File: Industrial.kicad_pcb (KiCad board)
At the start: 2 copper layers, 101.6 x 39.4 mm, 17 parts, among them J1 ASC712, J2 INA219, J3 Corriente, Q1 TIC106, U1 H11AA1, U2 MOC3052M, U3 Esp32

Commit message: fix pcb
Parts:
- moved Q1 56.9 mm to (194.6, 111.8), turned to 90 degrees
- moved J3 37.3 mm to (175.5, 82.3), turned to 90 degrees
- moved R6 28.1 mm to (181.4, 101.1)
- moved R2 27.5 mm to (153.7, 129.0)
- moved R3 26.8 mm to (167.6, 129.0)
- moved U1 21.8 mm to (160.5, 117.1)
- moved R4 21.6 mm to (181.9, 119.4)
- moved D1 18.3 mm to (181.1, 128.0)
- moved R5 17.4 mm to (165.6, 93.0)
- moved U2 16.1 mm to (167.4, 101.6)
- moved J1 16.0 mm to (161.3, 82.3)
- moved L1 15.2 mm to (197.9, 133.3)
- moved R1 14.5 mm to (154.4, 111.0)
- moved S1 13.8 mm to (141.7, 99.8)
- moved J2 13.4 mm to (138.9, 82.0)
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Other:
- board size 101.6 x 39.4 mm -> 100.3 x 61.7 mm

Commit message: finish first version
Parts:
- removed J3: Corriente, Connector_PinHeader_2.54mm:PinHeader_1x02_P2.54mm_Vertical
- added J4: Corriente, Connector_PinHeader_2.54mm:PinHeader_1x02_P2.54mm_Vertical, F.Cu at (197.4, 97.8)
- Q1: footprint Package_TO_SOT_THT:TO-220-3_Vertical -> TerminalBlock:TerminalBlock_bornier-3_P5.08mm
- moved J1 54.6 mm to (142.5, 133.6)
- moved R2 37.8 mm to (184.7, 107.4), turned to 180 degrees
- moved R4 34.4 mm to (149.6, 107.4), turned to 180 degrees
- moved R1 32.2 mm to (185.4, 119.6), turned to 180 degrees
- moved S1 29.1 mm to (170.7, 97.3), turned to 90 degrees
- moved R5 21.0 mm to (145.0, 88.9), turned to 180 degrees
- moved R3 19.1 mm to (150.1, 121.4), turned to 180 degrees
- moved U2 17.0 mm to (152.9, 92.7)
- moved R6 16.8 mm to (165.4, 106.2), turned to 180 degrees
- moved J2 15.5 mm to (154.4, 81.3)
- moved D1 9.41 mm to (171.7, 128.5)
- moved U1 7.68 mm to (166.9, 121.4), turned to 180 degrees
- moved Q1 5.40 mm to (198.1, 115.8)
- moved U3 1.83 mm to (117.9, 103.1)
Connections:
- net /notA renamed Net-(S1-Pad2)
- J2 pad 1: /Vcc -> /5v
- Q1 pad 1: /Battery -> Net-(J4-Pad1)
- S1 pad 1: /Vcc -> Net-(S1-Pad1)
- S1 pad 16: Net-(S1-Pad16) -> /5v
- U3 pad 32: Net-(U3-Pad32) -> GND
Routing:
- net /5v: track 0.00 -> 251.2 mm
- net GND: track 0.00 -> 212.7 mm, vias 0 -> 2
- net /Fase: track 0.00 -> 94.2 mm, vias 0 -> 2
- net /Vcc: track 0.00 -> 87.0 mm
- net /TrueZero: track 0.00 -> 70.1 mm, vias 0 -> 2
- net /Shoot: track 0.00 -> 65.0 mm
- net /ZeroCross: track 0.00 -> 54.7 mm
- net /Neutro: track 0.00 -> 50.8 mm
- net Net-(D1-Pad1): track 0.00 -> 47.9 mm
- net /SDA: track 0.00 -> 41.8 mm, vias 0 -> 2
- net /SCR: track 0.00 -> 35.5 mm
- net /SCL: track 0.00 -> 33.1 mm, vias 0 -> 2
- net Net-(R1-Pad1): track 0.00 -> 32.3 mm
- net /A0: track 0.00 -> 32.3 mm
- net Net-(R2-Pad1): track 0.00 -> 30.1 mm
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- added copper zone on B.Cu, net GND
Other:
- net class Juanda added: clearance 0.3, trace_width 0.9, via_dia 1, via_drill 0.8
- net class power added: clearance 0.4, trace_width 1.27, via_dia 1, via_drill 0.8
- net class señal added: clearance 0.3, trace_width 0.762, via_dia 1, via_drill 0.8
- board text added: "Cargador de baterias"
- board text added: "Ingenieria Electrónica UPB Juan David Barrero Luis David Calderon"

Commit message: finish but it can be better
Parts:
- added C1: 1000uF, Capacitor_THT:CP_Radial_D13.0mm_P5.00mm, F.Cu at (162.6, 142.2)
- added D2: D, Diode_THT:D_A-405_P7.62mm_Horizontal, F.Cu at (178.1, 145.8)
- added D3: LED, LED_THT:LED_D4.0mm, F.Cu at (108.0, 141.8)
- added J3: Conn_01x02, Connector_PinHeader_2.54mm:PinHeader_1x02_P2.54mm_Vertical, F.Cu at (134.4, 140.2)
- added R7: 440, Resistor_THT:R_Axial_DIN0309_L9.0mm_D3.2mm_P5.08mm_Vertical, F.Cu at (120.4, 142.7)
- added U4: LM7805_TO220, Package_TO_SOT_THT:TO-220-3_Vertical, F.Cu at (149.6, 133.3)
- moved J1 12.8 mm to (144.3, 146.3)
- moved L1 12.3 mm to (196.3, 145.5)
- moved Q1 5.86 mm to (196.3, 121.4)
- moved D1 5.73 mm to (177.3, 129.8)
- moved BT1 1.27 mm to (196.3, 87.4)
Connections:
- net Net-(D1-Pad1) renamed /bridge
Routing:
- net /5v: track 251.2 -> 132.9 mm, vias 0 -> 2
- net /Fase: track 94.2 -> 177.5 mm
- net Net-(C1-Pad1): track 0.00 -> 39.8 mm
- net /TrueZero: track 70.1 -> 103.7 mm, vias 2 -> 0
- net Net-(J3-Pad2): track 0.00 -> 33.1 mm
- net GND: track 212.7 -> 242.8 mm, vias 2 -> 4
- net /A0: track 32.3 -> 60.1 mm, vias 0 -> 2
- net /Shoot: track 65.0 -> 41.5 mm, vias 0 -> 2
- net /Vcc: track 87.0 -> 108.7 mm
- net /SDA: track 41.8 -> 63.4 mm, vias 2 -> 0
- net /Neutro: track 50.8 -> 69.8 mm
- net Net-(J4-Pad1): track 20.3 -> 33.7 mm, vias 0 -> 2
- net Net-(R1-Pad1): track 32.3 -> 19.3 mm
- net Net-(D3-Pad2): track 0.00 -> 10.3 mm
- net Net-(R6-Pad2): track 10.9 -> 21.1 mm, vias 0 -> 2
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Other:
- board size 100.3 x 61.7 mm -> 100.3 x 73.7 mm

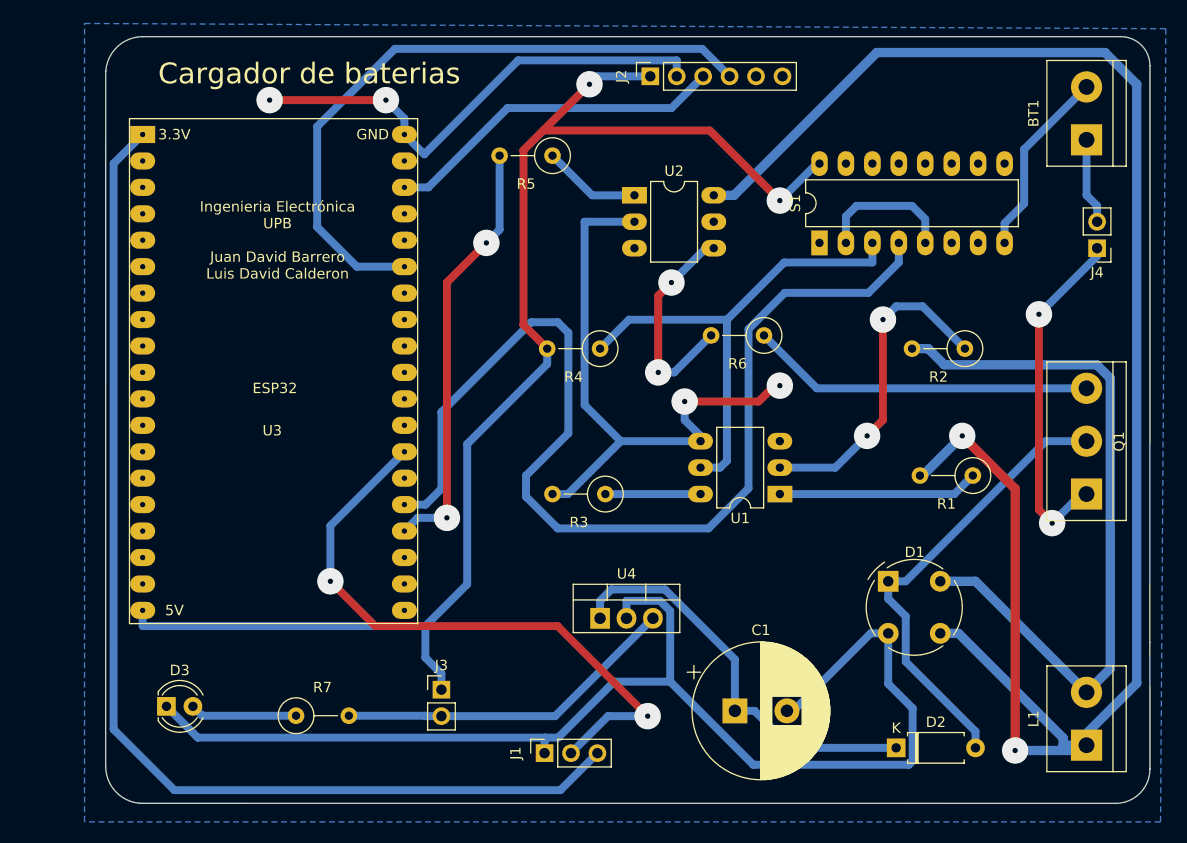
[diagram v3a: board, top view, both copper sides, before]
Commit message: final desing with adc pin 24
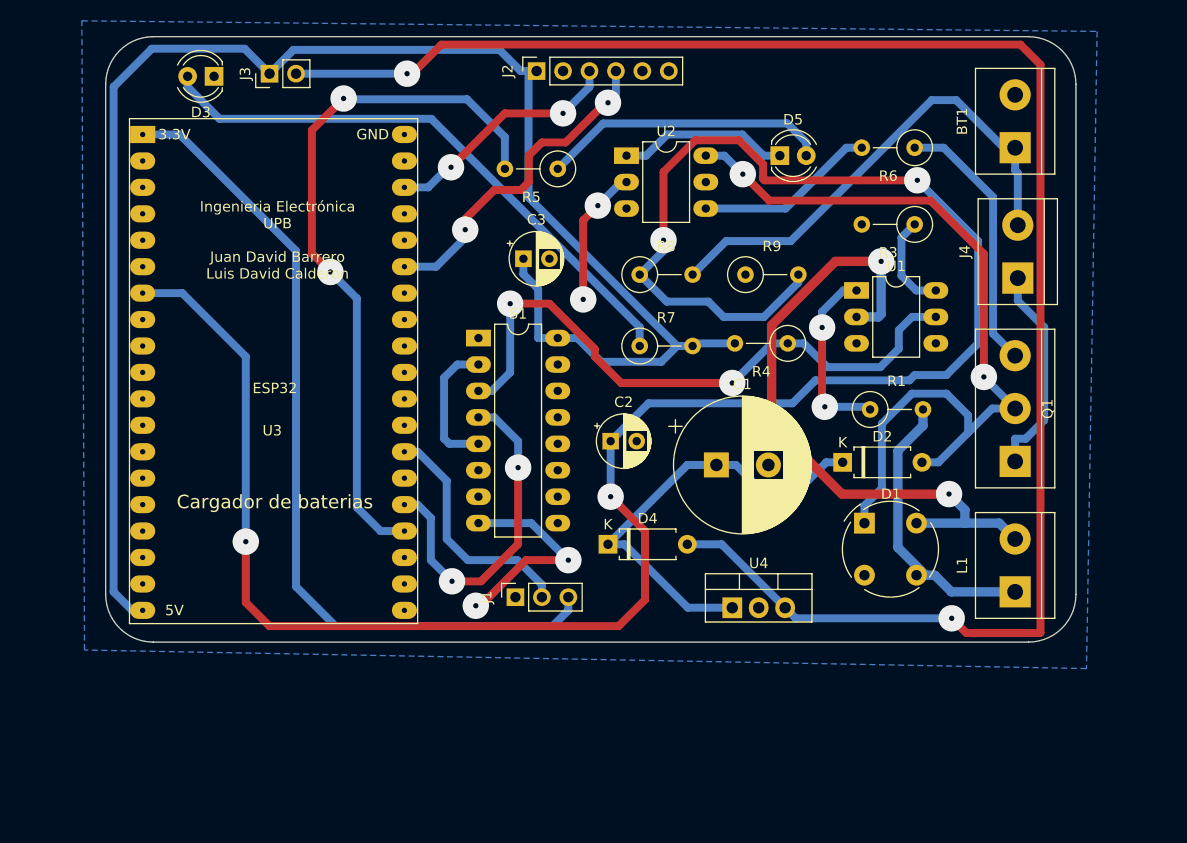
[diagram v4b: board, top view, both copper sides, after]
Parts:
- removed R2: 1.5K, Resistor_THT:R_Axial_DIN0309_L9.0mm_D3.2mm_P5.08mm_Vertical
- added C2: 10uF, Capacitor_THT:CP_Radial_D5.0mm_P2.50mm, F.Cu at (150.6, 116.3)
- added C3: 10uF, Capacitor_THT:CP_Radial_D5.0mm_P2.50mm, F.Cu at (142.2, 98.8)
- added D4: D, Diode_THT:D_A-405_P7.62mm_Horizontal, F.Cu at (150.4, 126.2)
- added D5: LED, LED_THT:LED_D4.0mm, F.Cu at (166.9, 88.9)
- added R8: 10k, Resistor_THT:R_Axial_DIN0309_L9.0mm_D3.2mm_P5.08mm_Vertical, F.Cu at (153.4, 100.3)
- added R9: 10k, Resistor_THT:R_Axial_DIN0309_L9.0mm_D3.2mm_P5.08mm_Vertical, F.Cu at (163.6, 100.3)
- J4: footprint Connector_PinHeader_2.54mm:PinHeader_1x02_P2.54mm_Vertical -> TerminalBlock:TerminalBlock_bornier-2_P5.08mm
- moved J3 61.4 mm to (117.9, 81.0), turned to 90 degrees
- moved D3 60.7 mm to (112.5, 81.3), turned to 180 degrees
- moved R7 48.5 mm to (153.4, 107.2)
- moved R3 39.4 mm to (179.8, 95.5)
- moved S1 34.0 mm to (137.9, 106.4), turned to 0 degrees
- moved D2 27.9 mm to (172.9, 118.4)
- moved C1 23.7 mm to (160.8, 118.6)
- moved R6 23.1 mm to (179.8, 88.1)
- moved U1 20.9 mm to (174.2, 101.9), turned to 0 degrees
- moved R4 18.0 mm to (167.6, 106.9)
- moved L1 16.3 mm to (189.5, 130.8)
- moved J1 15.2 mm to (141.5, 131.3)
- moved U4 12.7 mm to (162.3, 132.3)
- moved R1 11.7 mm to (175.6, 113.3), turned to 0 degrees
- moved J2 10.9 mm to (143.5, 80.8)
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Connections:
- J3 pad 2: Net-(J3-Pad2) -> Net-(D4-Pad2)
- R5 pad 1: Net-(R5-Pad1) -> Net-(D5-Pad2)
- R7 pad 2: Net-(J3-Pad2) -> /5v
- U1 pad 2: Net-(R2-Pad1) -> /Neutro
- U2 pad 1: Net-(R5-Pad1) -> Net-(D5-Pad1)
- U2 pad 6: /Fase -> /bridge
- U3 pad 7: Net-(U3-Pad7) -> /Bat_adc
- U4 pad 3: Net-(J3-Pad2) -> Net-(D4-Pad2)
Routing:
- net GND: track 242.8 -> 34.1 mm
- net /Bat_adc: track 0.00 -> 208.2 mm, vias 0 -> 4
- net Net-(D4-Pad2): track 0.00 -> 165.9 mm, vias 0 -> 2
- net /Fase: track 177.5 -> 28.2 mm, vias 2 -> 0
- net /TrueZero: track 103.7 -> 32.5 mm, vias 0 -> 2
- net Net-(D3-Pad2): track 10.3 -> 55.8 mm
- net /Battery: track 8.29 -> 47.8 mm
- net /A0: track 60.1 -> 23.0 mm, vias 2 -> 0
- net /bridge: track 44.1 -> 80.1 mm, vias 0 -> 2
- net Net-(J3-Pad2): track 33.1 -> 0.00 mm
- net Net-(R2-Pad1): track 31.5 -> 0.00 mm, vias 2 -> 0
- net /SDA: track 63.4 -> 32.0 mm, vias 0 -> 2
- net Net-(D5-Pad2): track 0.00 -> 27.7 mm
- net /Vcc: track 108.7 -> 81.2 mm
- net /Shoot: track 41.5 -> 67.9 mm
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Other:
- board size 100.3 x 73.7 mm -> 93.2 x 58.2 mm
